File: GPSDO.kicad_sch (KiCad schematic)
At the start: 74 parts, among them J1 Conn_Coaxial, J2 GPS_CONN, J3 Conn_Coaxial, J4 Conn_Coaxial, J5 Conn_Coaxial, J6 Conn_Coaxial, J7 LCD_CONN, J8 Barrel_Jack, J9 TOUCH_CONN, SW1 RESET_BTN, U1 REF3450, U11 74AUC1G74, U14 MC3487DX, U16 L7805, U2 74AUC1G125, U3 AD5680, U4 NB3N551MN, U5 LTC2050IS8, U6 AVR32DB28x-xSO, U7 74AUC1G125, U8 74HC390, X1 OCXO-14

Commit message: Updated schematic
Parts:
- removed C1, C17, C18, C9: 10u, Capacitor_THT:CP_Radial_D5.0mm_P2.00mm, symbol Device:C_Polarized_Small
- removed C10: 1u, Capacitor_THT:CP_Radial_D5.0mm_P2.00mm, symbol Device:C_Polarized_Small
- removed C36, C37, C38, C39, C40, C41, C42, C43: 0u1 10V, Capacitor_SMD:C_0805_2012Metric_Pad1.18x1.45mm_HandSolder, symbol Device:C_Polarized_Small
- removed U16: L7805, Package_TO_SOT_THT:TO-220-3_Vertical, symbol Regulator_Linear:L7805
- added C1, C10, C11: 100u 35V, Capacitor_SMD:C_Elec_6.3x7.7, symbol Device:C_Polarized
- added C17: 100n low ESR, Capacitor_SMD:C_0805_2012Metric_Pad1.18x1.45mm_HandSolder, symbol Device:C_Small
- added C18, C9: 10u 25V, Capacitor_SMD:C_1210_3225Metric_Pad1.33x2.70mm_HandSolder, symbol Device:C_Small
- added C19, C20: 100u 35V, Capacitor_SMD:CP_Elec_8x10, symbol Device:C_Polarized_Small
- added C28: 100n, Capacitor_SMD:C_0805_2012Metric_Pad1.18x1.45mm_HandSolder, symbol Device:C
- added C29, C30, C36, C37, C38, C39, C40, C41: 100n 10V MLCC, Capacitor_SMD:C_0805_2012Metric_Pad1.18x1.45mm_HandSolder, symbol Device:C_Small
- added R11: 0R, Resistor_SMD:R_0805_2012Metric_Pad1.20x1.40mm_HandSolder, symbol Device:R_Small_US
- added U10: MC7805BDTRKG, Package_TO_SOT_SMD:TO-252-2, symbol Regulator_Linear:LM78M05_TO252
- added U9: L7805CV, Package_TO_SOT_THT:TO-220-3_Horizontal_TabDown, symbol Regulator_Linear:L7805
- C22: value 10u -> 100u 35V; footprint Capacitor_SMD:C_Elec_4x5.4 -> Capacitor_SMD:C_Elec_6.3x7.7
- C32, C33, C34: value 100u -> 100u 35V; footprint Capacitor_THT:CP_Radial_D5.0mm_P2.00mm -> Capacitor_SMD:CP_Elec_8x10
- C5: value 10u -> 100u 35V; footprint Capacitor_THT:CP_Radial_D5.0mm_P2.00mm -> Capacitor_SMD:CP_Elec_8x10
- C7: value tot=15pF? -> total OCXO load=15pF?
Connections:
- net +5VA: now also C33.1, C34.1, C35.2, C5.1, C1.1, C11.1, U9.3 (OUT)
- net +5VD: now also C10.1, C20.1, C28.2, U10.3 (VO); no longer C33.1, C34.1, C35.2
- net GND: now also C10.2, C19.2, C20.2, C28.1, R11.1, U10.2 (GND); no longer C32.2, C33.2, C34.2, C35.1, J8.2
- net GNDA: now also C32.2, C33.2, C34.2, C35.1, J8.2, C1.2, C11.2, C17.2, C18.2, C9.2, R11.2, U9.2 (GND)
- net at R3.2, U5.3 (+): now also C17.1, C18.1
- net at J6.1 (In): now also C40.2
- net at U14.13 (OUT-): now also C40.1
- net at J3.2 (Ext): now also C30.2
- net at U14.2 (OUT+): now also C30.1
- net at J4.2 (Ext): now also C37.2
- net at U14.6 (OUT+): now also C37.1
- net at U14.14 (OUT+): now also C41.1
- net at J4.1 (In): now also C36.2
- net at U14.5 (OUT-): now also C36.1
- net at U14.10 (OUT+): now also C39.1
- net at U14.11 (OUT-): now also C38.1
- net at J5.1 (In): now also C38.2
- net at J6.2 (Ext): now also C41.2
- net at C3.1, U1.5 (OUT_S), U1.6 (OUT_F)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: now also C9.1; no longer C5.1
- net 7VIN: now reaches C32.1, J8.1
- net 7VIN: now also C19.1, U10.1 (VI), U9.1 (IN)
- net at U14.3 (OUT-): now also C29.1
- net at J3.1 (In): now also C29.2
- net at J5.2 (Ext): now also C39.2
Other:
- note added: "Analog 100u 35V VZL101M1VTR-0810 8 Diam 10 L 0.16 Ohm 600 mA Digital 100u 35V VZL101M1VTR-0607 6.3 Diam 7.7 L 0.32 Ohm 290 mA DAC 10u 25V KAM32LL81E106KU 1210"
- note added: "TODO: - where to put trigger pin? - where to put ADC pin? -clock gen pow supply - check everything ok opn 5V? - (touch) display - serial interface -"
- note added: "TODO: Decoupling caps for 10Mc with series resonance well above 100Mc"
- note removed: "Notes: - no SS for SPI ... using PCINT11 - no UART: using DI/DO for RX/TX maybe reusable"
- note removed: "TODO: -Time counter circuit for AVR32DB48 - not gates necessary? - where to put trigger pin? - where to put ADC pin? -mounting holes -CD4040 vs 4020 -connector align display -UART_RX & TX -clock gen pow supply - check everything ok opn 5V? - CHG_ENABLE: next buffer floating? - LM311 unused pins - (touch) display - serial interface -"
- moved on the sheet: C16, C32, C33, C34, C35, C6, J2, J7, J8, J9, U5

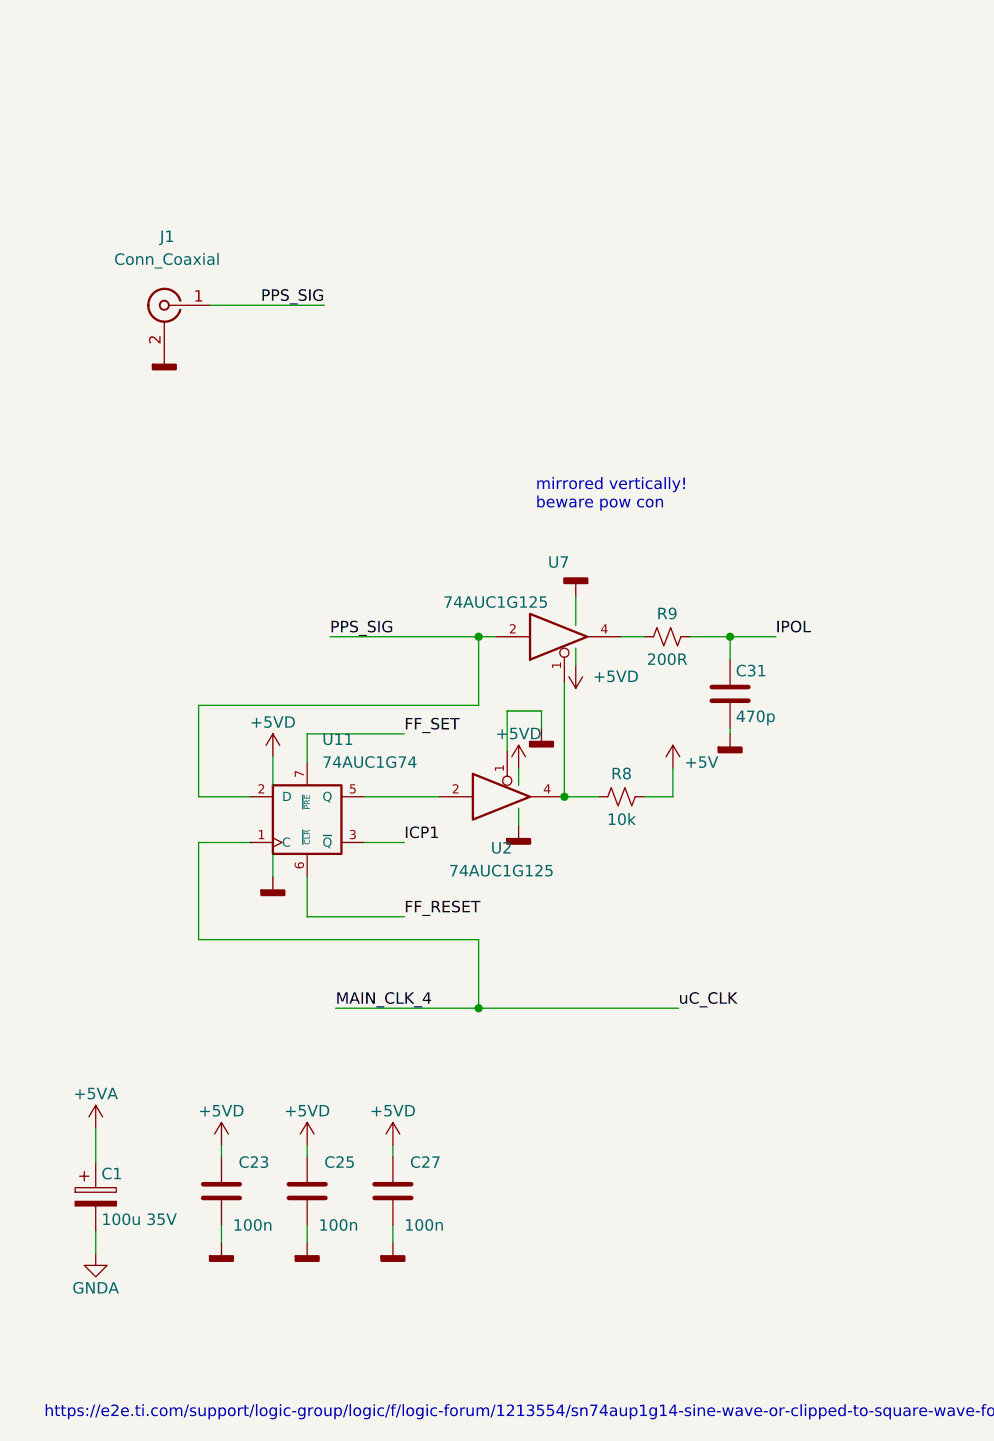
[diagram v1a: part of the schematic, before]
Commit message: Added pulse delay in TIC
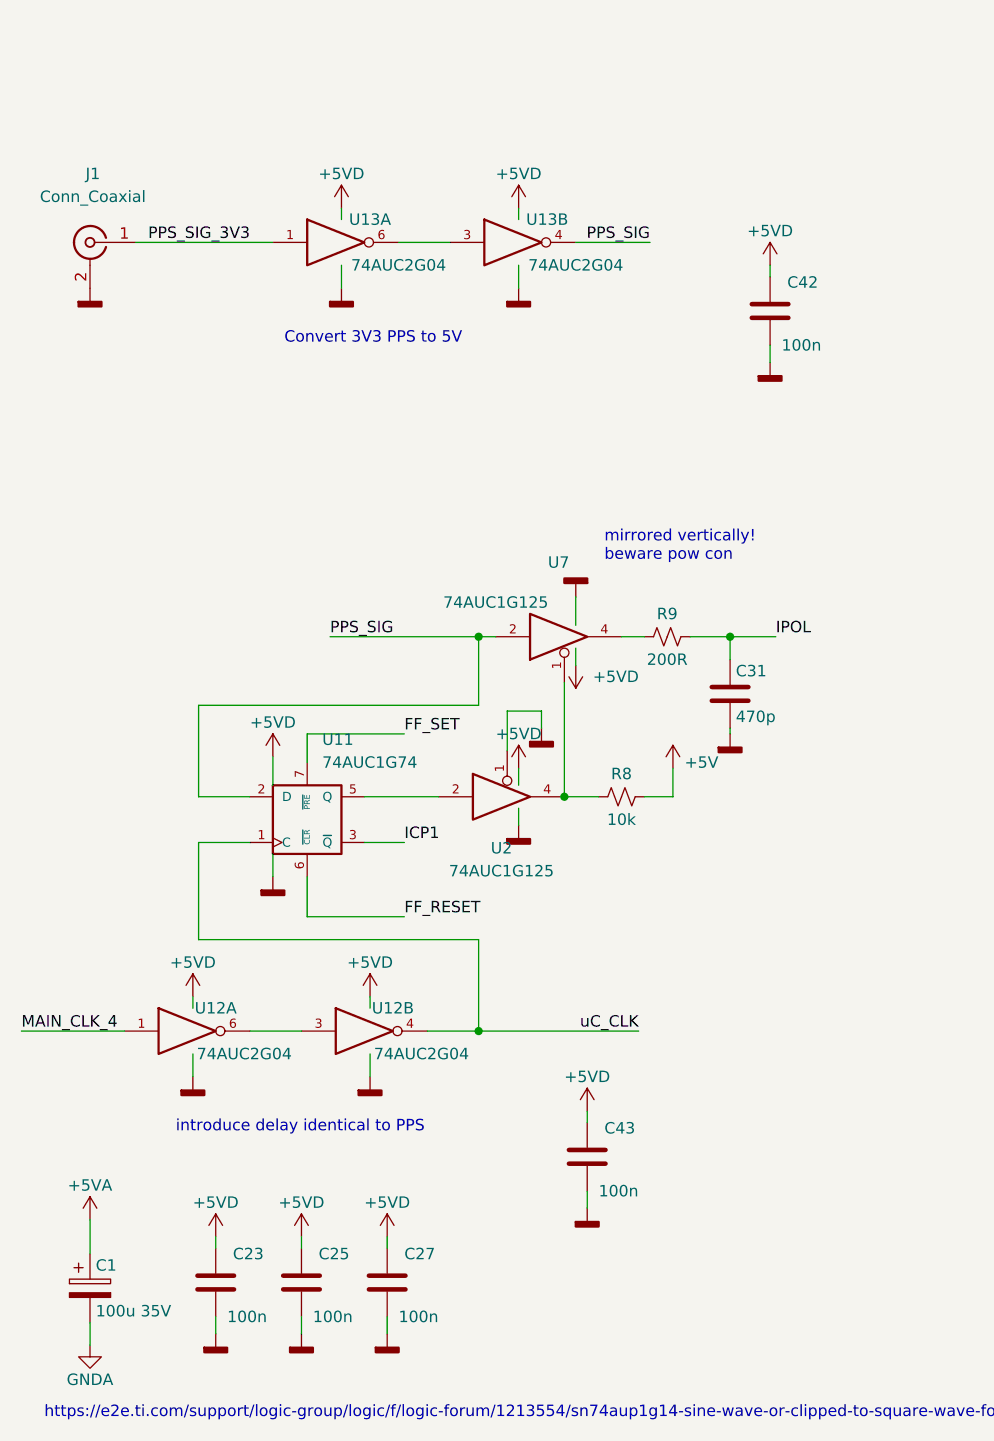
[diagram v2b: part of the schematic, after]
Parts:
- added C42, C43: 100n, Capacitor_SMD:C_0805_2012Metric_Pad1.18x1.45mm_HandSolder, symbol Device:C
- added U12, U13: 74AUC2G04, Package_SO:TSOP-6_1.65x3.05mm_P0.95mm, symbol 74xGxx:74AUC2G04
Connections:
- net +5VD: now also C42.2, C43.2, U12.5 (VCC), U12.5 (VCC), U13.5 (VCC), U13.5 (VCC)
- net GND: now also C42.1, C43.1, U12.2 (GND), U12.2 (GND), U13.2 (GND), U13.2 (GND)
- net MAIN_CLK_4: now also U12.1; no longer U11.1 (C), U6.22 (XTALHF1/PA0)
- net PPS_SIG: now also U13.4; no longer J1.1 (In)
- new net: U12.3, U12.6
- new net: U13.3, U13.6
- new net PPS_SIG_3V3: J1.1 (In), U13.1
- new net uC_CLK: U11.1 (C), U12.4, U6.22 (XTALHF1/PA0)
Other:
- note added: "Convert 3V3 PPS to 5V"
- note added: "introduce delay identical to PPS"
- moved on the sheet: C1, C23, C25, C27, J1

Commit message: selected TIC components
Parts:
- removed C8: 1u, Capacitor_SMD:C_0805_2012Metric_Pad1.18x1.45mm_HandSolder, symbol Device:C_Polarized_Small
- removed R5, R7: 2k2, Resistor_SMD:R_0805_2012Metric_Pad1.20x1.40mm_HandSolder, symbol Device:R_Small_US
- added C8: 1u, Capacitor_SMD:C_0805_2012Metric_Pad1.18x1.45mm_HandSolder, symbol Device:C_Small
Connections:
- net +5VD: now also J2.1 (Pin_1)
- net GND: now also J2.4 (Pin_4), C8.2
- net GPS_RXD: now also J2.3 (Pin_3)
- net GPS_TXD: now also J2.2 (Pin_2)
- net ~{RESET}: now also C8.1
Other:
- note added: "add cap multiplier ?"
- moved on the sheet: C42, J2, J7, J9

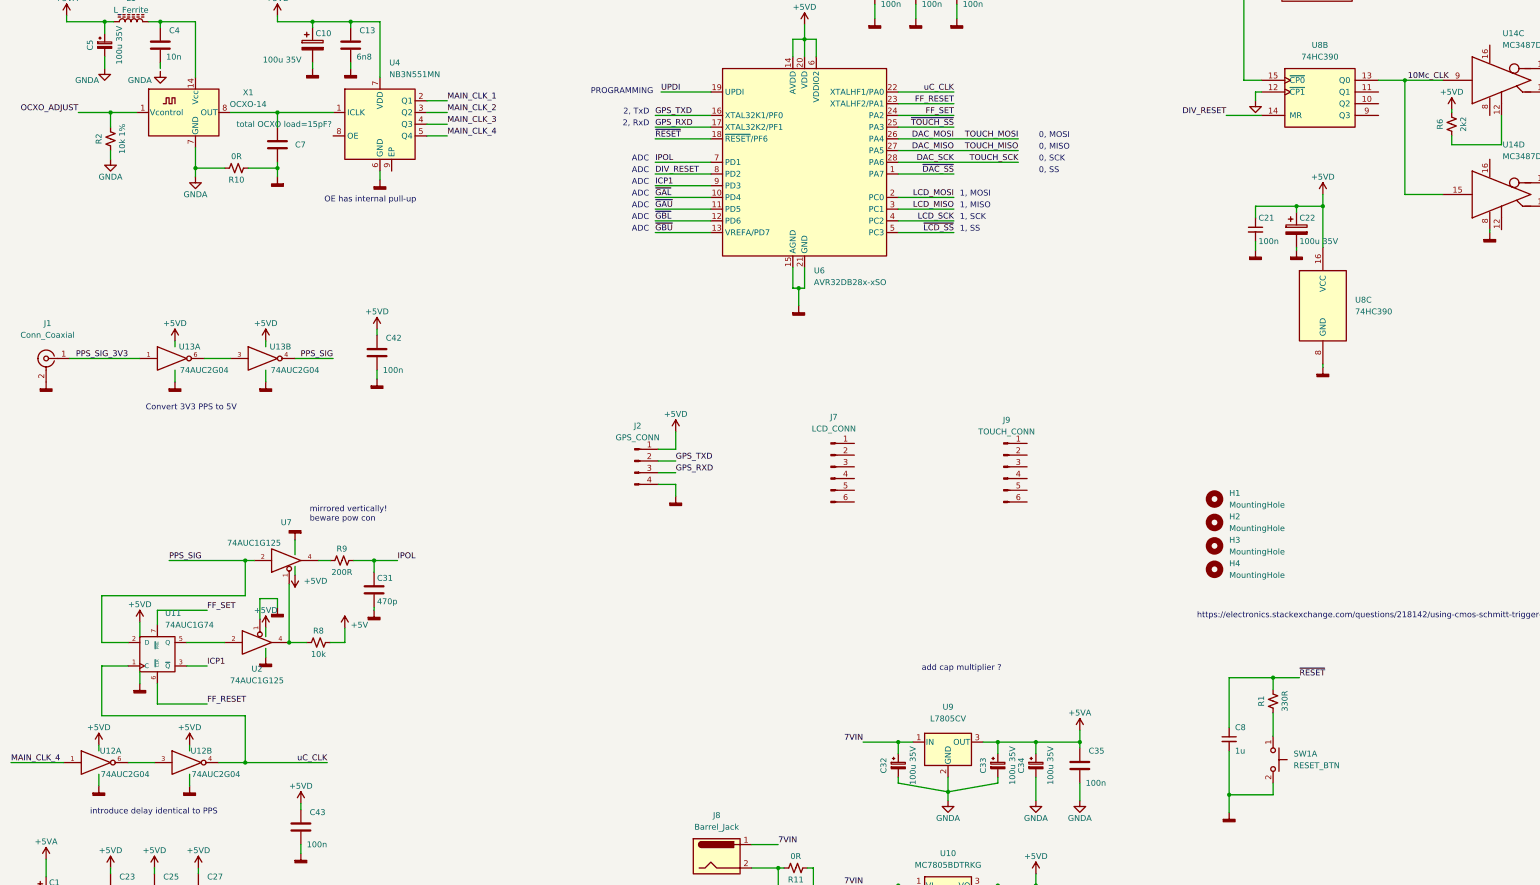
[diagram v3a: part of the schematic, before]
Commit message: Added LEDs, modified SPI
All SPI uses the same interface now.
Added extra clocksource to a gpio pin, I don't know whether the internal systick timer will be configurable enough to count ticks
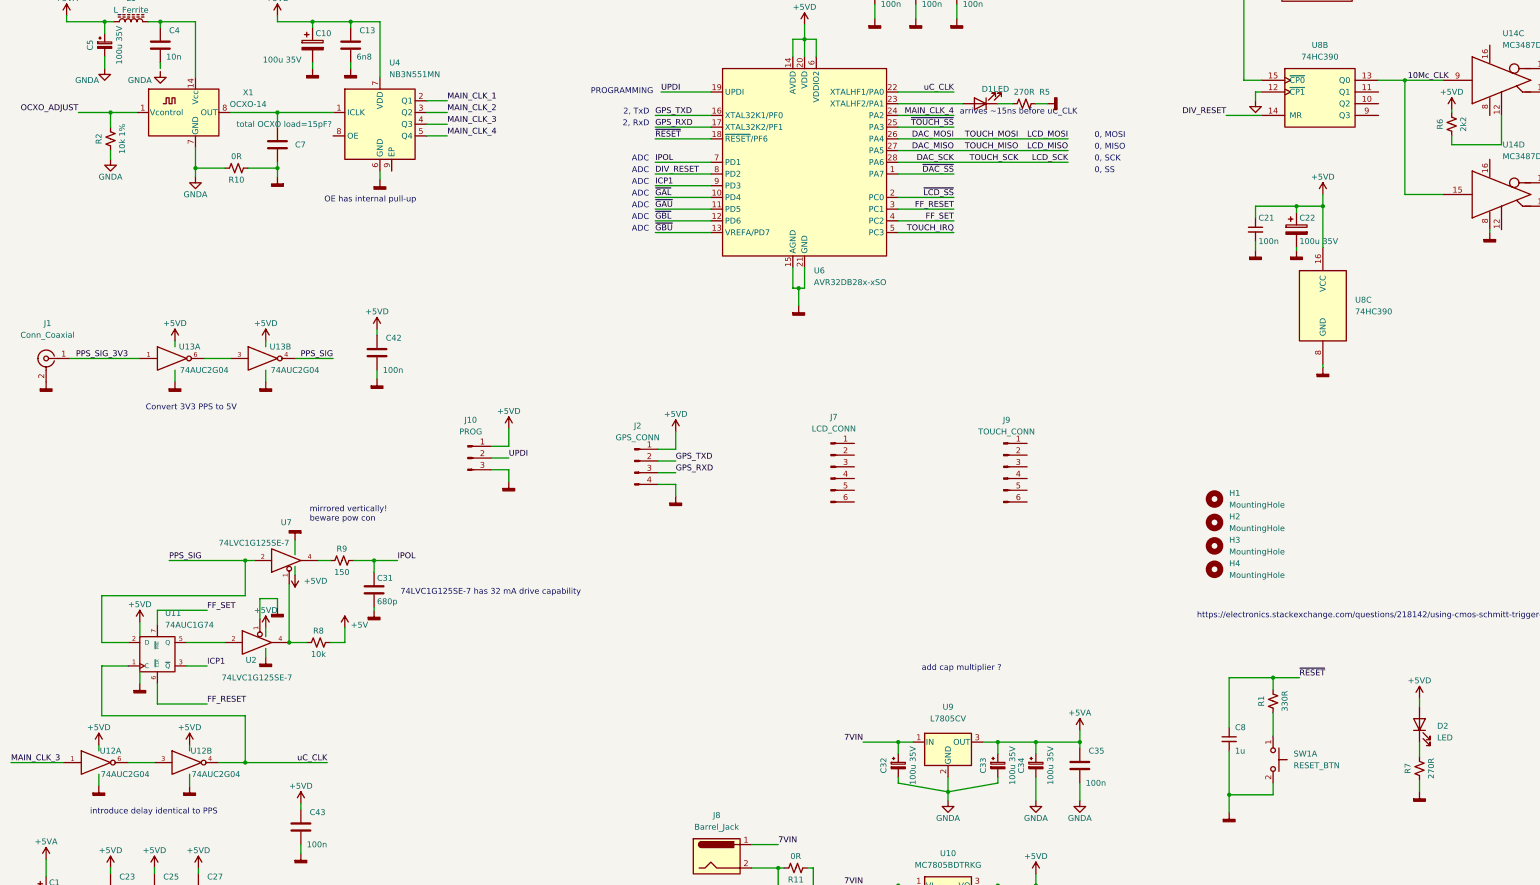
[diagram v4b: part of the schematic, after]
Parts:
- added D1, D2: LED, LED_SMD:LED_0805_2012Metric, symbol Device:LED
- added J10: PROG, Connector_PinHeader_2.54mm:PinHeader_1x03_P2.54mm_Vertical, symbol Connector:Conn_01x03_Male
- added R5, R7: 270R, Resistor_SMD:R_0805_2012Metric_Pad1.20x1.40mm_HandSolder, symbol Device:R_Small_US
- C31: value 470p -> 680p
- R9: value 200R -> 150
- U2, U7: value 74AUC1G125 -> 74LVC1G125SE-7; footprint Package_TO_SOT_SMD:SOT-23-5_HandSoldering -> Package_TO_SOT_SMD:SOT-353_SC-70-5
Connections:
- net LCD_MISO is gone; now on net FF_RESET: U6.3 (PC1)
- net LCD_MOSI is gone; now on net ~{LCD_SS}: U6.2 (PC0)
- net LCD_SCK is gone; now on net FF_SET: U6.4 (PC2)
- net +5VD: now also D2.2 (A), J10.1 (Pin_1)
- net FF_RESET: no longer U6.23 (XTALHF2/PA1)
- net FF_SET: no longer U6.24 (PA2)
- net GND: now also J10.3 (Pin_3), R5.1, R7.1
- net MAIN_CLK_3: now also U12.1
- net MAIN_CLK_4: now also U6.24 (PA2); no longer U12.1
- net UPDI: now also J10.2 (Pin_2)
- net ~{LCD_SS}: no longer U6.5 (PC3)
- new net: D1.1 (K), R5.2
- new net: D1.2 (A), U6.23 (XTALHF2/PA1)
- new net: D2.1 (K), R7.2
- new net TOUCH_IRQ: U6.5 (PC3)
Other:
- note added: "74LVC1G125SE-7 has 32 mA drive capability"
- note added: "arrives ~15ns before uC_CLK"
- note removed: "1, MISO"
- note removed: "1, MOSI"
- note removed: "1, SCK"
- note removed: "1, SS"

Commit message: some pcb placing
finding optimal location on the pcb
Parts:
- C7: value total OCXO load=15pF? -> 10pF
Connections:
- net +5V is gone; now on net +5VD: R8.2
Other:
- note added: "Total capacitance seen by OCXO = 15pF"
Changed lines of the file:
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@@
     (effects (font (size 1.27 1.27)) (justify left bottom))
   )
+  (text "Total capacitance\nseen by OCXO = 15pF\n" (at 60.325 103.505 0)
+    (effects (font (size 1.27 1.27)) (justify left bottom))
+  )
   (text "introduce delay identical to PPS" (at 30.48 250.825 0)
     (effects (font (size 1.27 1.27)) (justify left bottom))
@@
     (pin "8")
   )
-  (symbol (lib_id "power:+5V") (at 85.725 210.185 0) (unit 1)
-    (in_bom yes) (on_board yes)
-    (property "Reference" "#PWR0120" (id 0) (at 85.725 213.995 0)
-      (effects (font (size 1.27 1.27)) hide)
-    )
-    (property "Value" "+5V" (id 1) (at 88.9 209.55 0))
-    (property "Footprint" "" (id 2) (at 85.725 210.185 0)
-      (effects (font (size 1.27 1.27)) hide)
-    )
-    (property "Datasheet" "" (id 3) (at 85.725 210.185 0)
-      (effects (font (size 1.27 1.27)) hide)
-    )
-    (pin "1")
-  )
   (symbol (lib_id "Connector:Conn_Coaxial") (at 378.46 111.76 0) (unit 1)
     (in_bom yes) (on_board yes) (fields_autoplaced)
@@
       (effects (font (size 1.27 1.27)) (justify right))
     )
-    (property "Value" "total OCXO load=15pF?" (id 1) (at 62.23 100.965 0)
+    (property "Value" "10pF" (id 1) (at 72.39 108.585 0)
       (effects (font (size 1.27 1.27)) (justify right))
     )
@@
     (pin "8")
   )
+  (symbol (lib_id "power:+5VD") (at 85.725 210.185 0) (unit 1)
+    (in_bom yes) (on_board yes)
+    (property "Reference" "#PWR0120" (id 0) (at 85.725 213.995 0)
+      (effects (font (size 1.27 1.27)) hide)
+    )
+    (property "Value" "+5VD" (id 1) (at 86.995 210.82 0)
+      (effects (font (size 1.27 1.27)) (justify left))
+    )
+    (property "Footprint" "" (id 2) (at 85.725 210.185 0)
+      (effects (font (size 1.27 1.27)) hide)
+    )
+    (property "Datasheet" "" (id 3) (at 85.725 210.185 0)
+      (effects (font (size 1.27 1.27)) hide)
+    )
+    (pin "1")
+  )
   (symbol (lib_id "power:GNDD") (at 235.585 278.765 0) (unit 1)
     (in_bom yes) (on_board yes) (fields_autoplaced)
@@
       (reference "#PWR0119") (unit 1) (value "+5VD") (footprint "")
     )
-    (path "/5c147744-991d-4549-a0cc-ed1cace09740"
-      (reference "#PWR0120") (unit 1) (value "+5V") (footprint "")
+    (path "/dc4a32ff-2cd1-4a27-9ccf-6829e740dd6d"
+      (reference "#PWR0120") (unit 1) (value "+5VD") (footprint "")
     )
     (path "/9a277492-a4b0-4236-8014-fcd921169440"
@@
     )
     (path "/a7299b49-528f-4351-88a8-f97af480c3b7"
-      (reference "C7") (unit 1) (value "total OCXO load=15pF?") (footprint "Capacitor_SMD:C_0805_2012Metric_Pad1.18x1.45mm_HandSolder")
+      (reference "C7") (unit 1) (value "10pF") (footprint "Capacitor_SMD:C_0805_2012Metric_Pad1.18x1.45mm_HandSolder")
     )
     (path "/5a8db1ea-4e60-4a29-83ef-417281528736"
